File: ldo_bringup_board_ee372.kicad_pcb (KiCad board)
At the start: 4 copper layers, 100 x 100 mm, 152 parts, among them J1 VIN, J10 MD_SW_EN, J11 MD_MCU_PU_EN, J12 BUF_EN, J13 VSIG, J14 VSIG_BUF, J15 NR, J16 NOISE_X100, J17 NOISE_X1000, J18 VIN_PROBE, J19 VREF_PROBE, J2 GND, J20 VOUT_PROBE, J21 VG0_PROBE, J22 VG1_PROBE, J23 VG2_PROBE, J24 VG3_PROBE, J25 VG4_PROBE, J3 IBIAS, J4 VOUT, J5 VIN_SMA, J6 VOUT_SMA, J7 GND, J8 5V, J9 MD_MCU_EN, Q1 FDV305N, Q2 FDV305N, Q3 FDV305N, Q4 FDV305N, Q5 FDV305N, Q6 FDV305N, SW1 MD_SW, U1 LDO_DualMode_BGR_EE372, U2 Teensy4.1, U3 INA190A5IDDFR, U4 INA190A5IDDFR, U5 OPA4388IDR, U6 BUF602ID, U7 ADT7310TRZ

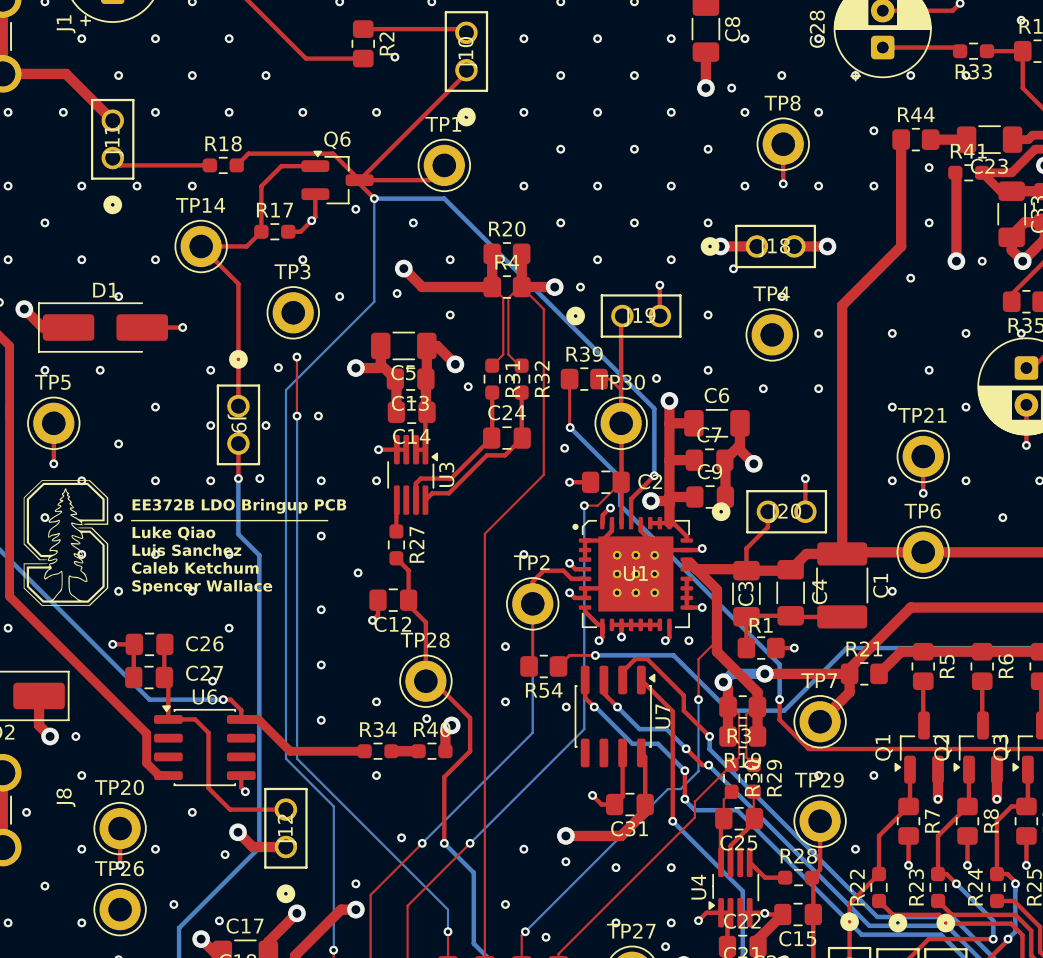
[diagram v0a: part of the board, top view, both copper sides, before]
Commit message: Move ground test points TP20, TP21 and TP8 next to TP26, TP6 and TP4
TP20 to (115.0, 117.5), TP21 to (169.5, 93.25), TP8 to (155.0, 84.75),
each within 4.6 mm of the signal test point it serves. Three GND stub
tracks that ended on the old pads and three GND stitching vias under the
new pads removed. Zones refilled.

DRC 0 errors, 0 unconnected, schematic parity 0.

Co-Authored-By: Claude Opus 5.5 (1M context) <noreply@anthropic.com>
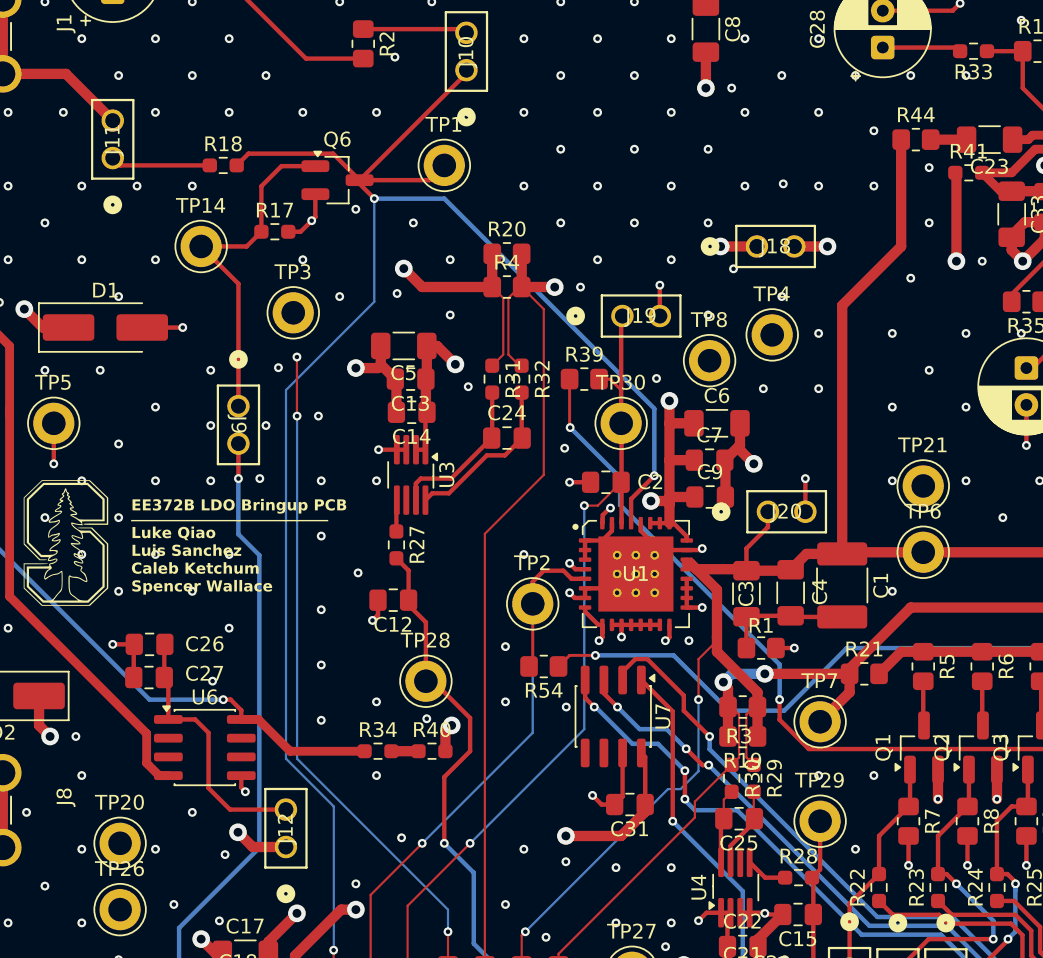
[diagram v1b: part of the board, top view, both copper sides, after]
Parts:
- moved TP8 15.5 mm to (155.0, 84.8)
- moved TP21 2.00 mm to (169.5, 93.2)
- moved TP20 1.00 mm to (115.0, 117.5)
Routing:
- net GND: track 238.8 -> 231.1 mm, vias 393 -> 390
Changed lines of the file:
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@@
 	(footprint "TestPoint:TestPoint_Keystone_5005-5009_Compact"
 		(layer "F.Cu")
-		(at 169.5 91.25)
+		(at 169.5 93.25)
 		(descr "Keystone THM Compact Test Point 5005-5009, http://www.keyelco.com/product-pdf.cfm?p=1314")
 		(tags "Through Hole Mount Test Points")
@@
 	(footprint "TestPoint:TestPoint_Keystone_5005-5009_Compact"
 		(layer "F.Cu")
-		(at 160 70.06)
+		(at 155 84.75)
 		(descr "Keystone THM Compact Test Point 5005-5009, http://www.keyelco.com/product-pdf.cfm?p=1314")
 		(tags "Through Hole Mount Test Points")
@@
 	(footprint "TestPoint:TestPoint_Keystone_5005-5009_Compact"
 		(layer "F.Cu")
-		(at 115 116.5)
+		(at 115 117.5)
 		(descr "Keystone THM Compact Test Point 5005-5009, http://www.keyelco.com/product-pdf.cfm?p=1314")
 		(tags "Through Hole Mount Test Points")
@@
 	)
 	(segment
-		(start 115 119)
-		(end 115 116.5)
-		(width 0.3)
-		(layer "F.Cu")
-		(net "GND")
-	)
-	(segment
 		(start 133.75 86.075)
 		(end 133.675 86)
@@
 	)
 	(segment
-		(start 169.5 93.75)
-		(end 169.5 91.25)
-		(width 0.3)
-		(layer "F.Cu")
-		(net "GND")
-	)
-	(segment
 		(start 132.125 102.375)
 		(end 132.5 102)
@@
 	)
 	(segment
-		(start 160 72.75)
-		(end 160 70.06)
-		(width 0.3)
-		(layer "F.Cu")
-		(net "GND")
-	)
-	(segment
 		(start 177.75 75.35)
 		(end 177.75 76.5)
@@
 	)
 	(via
-		(at 115 119)
-		(size 0.6)
-		(drill 0.3)
-		(layers "F.Cu" "B.Cu")
-		(net "GND")
-	)
-	(via
 		(at 131.15 99.15)
 		(size 0.6)
@@
 	)
 	(via
-		(at 154.9 85.4)
-		(size 0.6)
-		(drill 0.3)
-		(layers "F.Cu" "B.Cu")
-		(net "GND")
-	)
-	(via
 		(at 102.4 67.9)
 		(size 0.6)
@@
 		(size 0.6)
 		(drill 0.3)
-		(layers "F.Cu" "B.Cu")
-		(net "GND")
-	)
-	(via
-		(at 169.5 93.75)
-		(size 0.6)
-		(drill 0.3)
